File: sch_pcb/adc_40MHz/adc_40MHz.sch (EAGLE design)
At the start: 74 parts, among them IC1 AD9235BC, IC2 LT6600-15, IC3 LTC6254XMS, IC4 SN74LVC2G14DBV, IC5 LT1521XST, IC6 SN74LVC2G14DBV, X1 SMA-142-0701-851/861, X2 SMA-142-0701-851/861

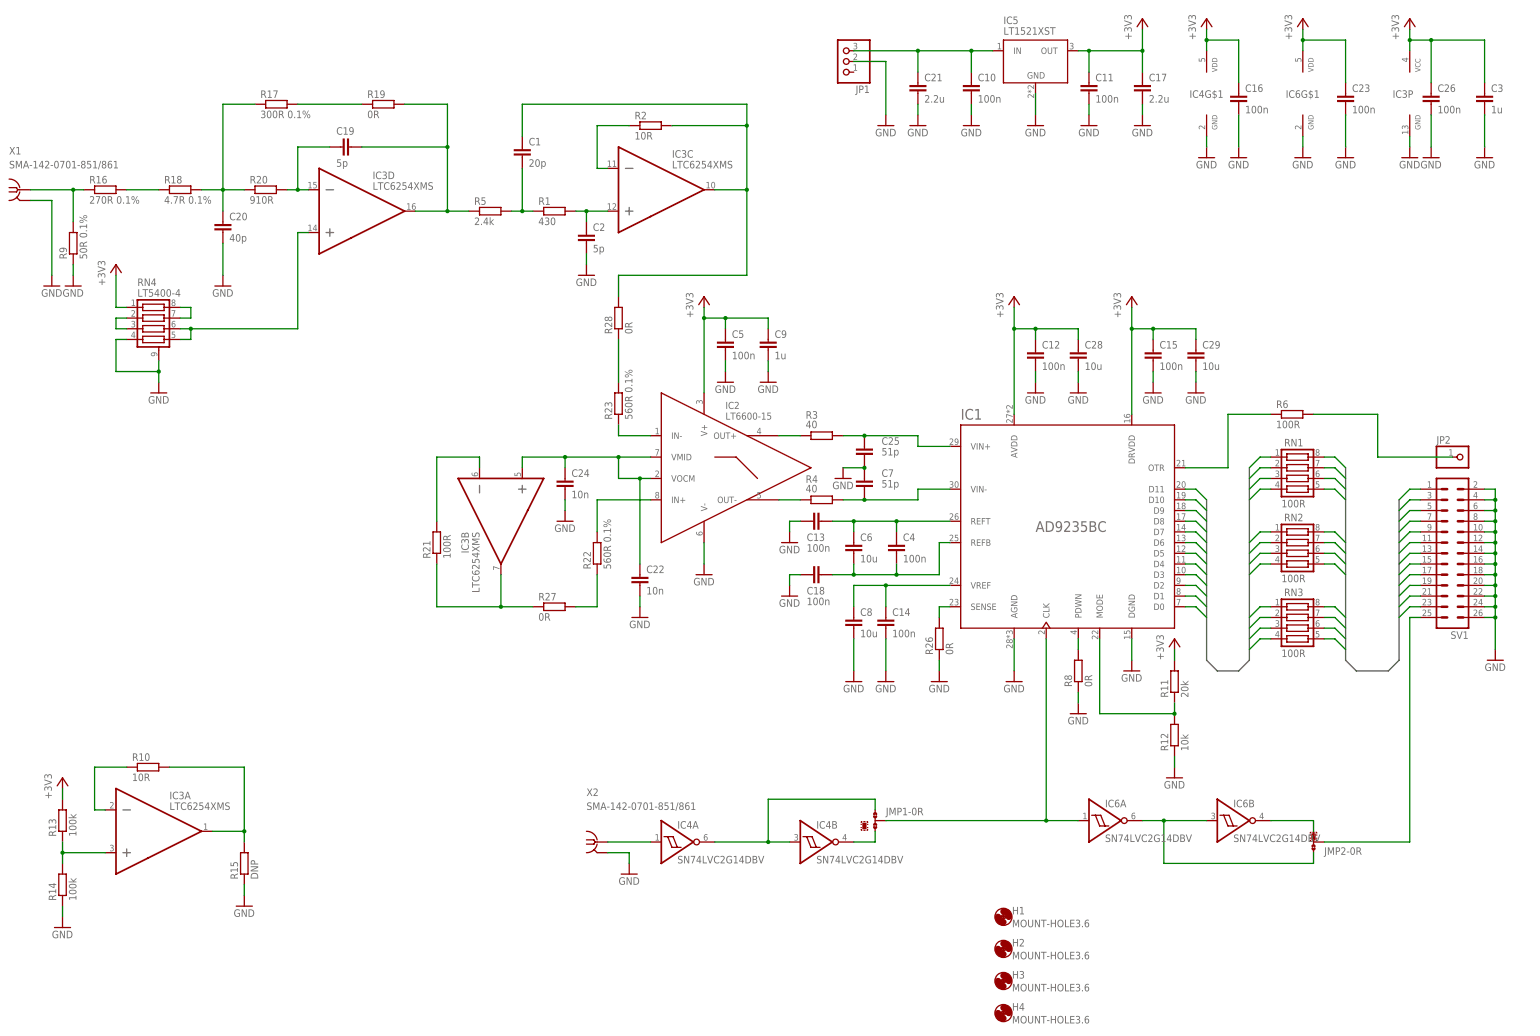
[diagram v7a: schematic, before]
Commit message: Dodano rezystory ustalające stan buforów. Sygnały w filrach skończone
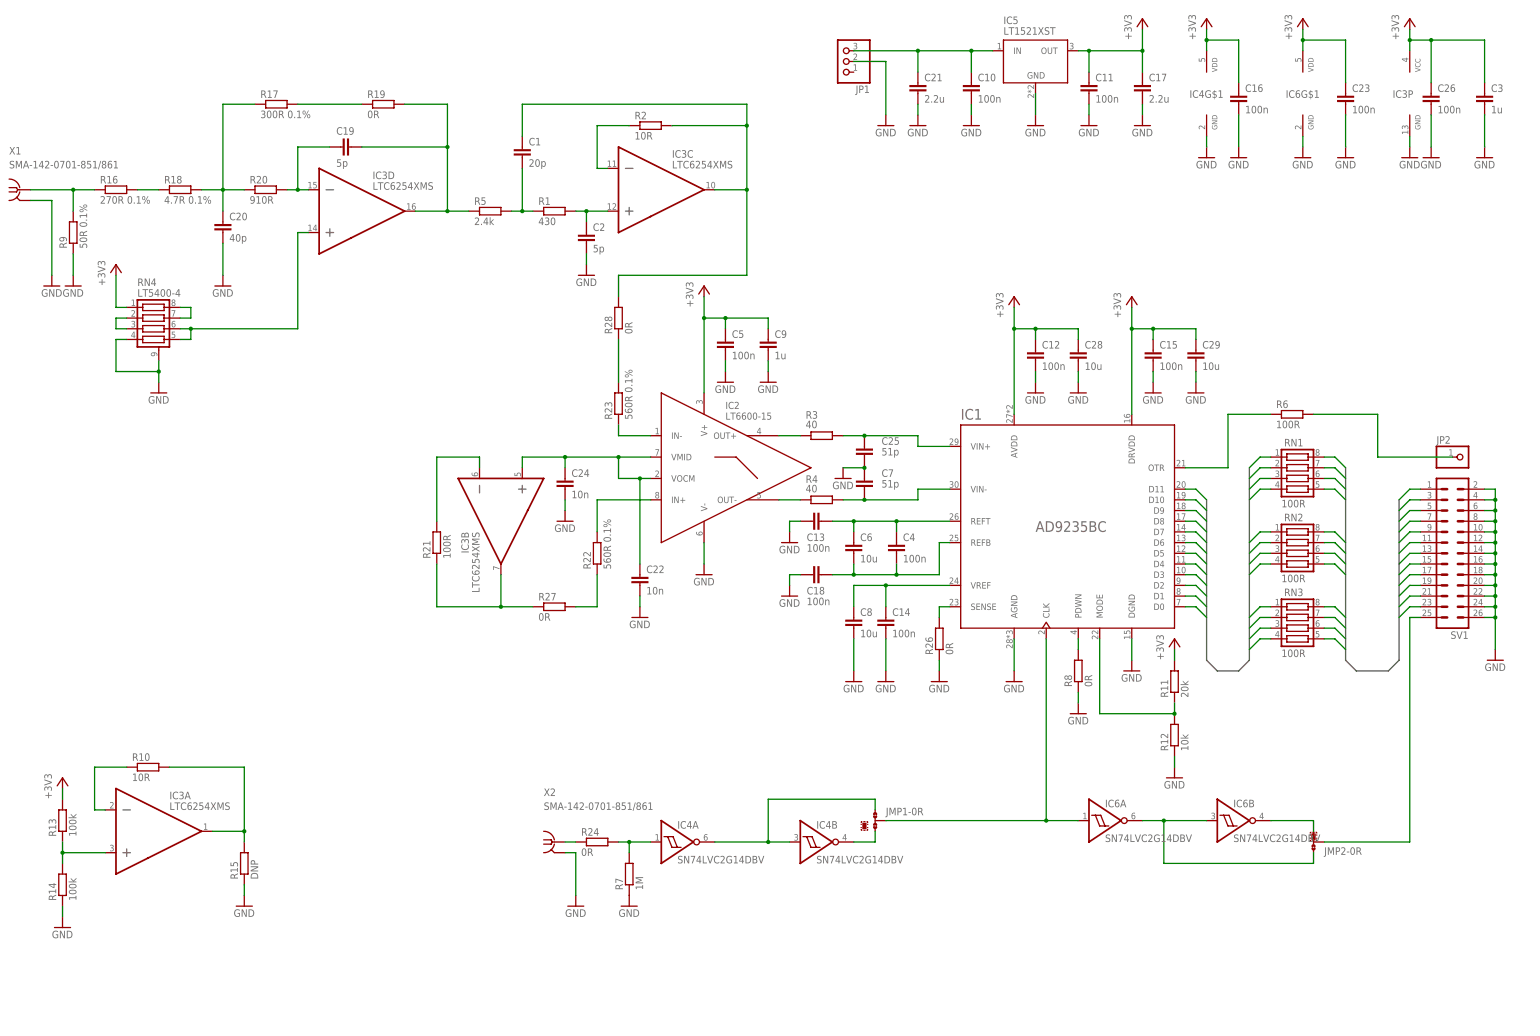
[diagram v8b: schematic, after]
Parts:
- removed H1, H2, H3, H4: MOUNT-HOLE3.6, holes:MOUNT-HOLE3.6
- added R24: 0R, rcl:R-EU_R0603
- added R7: 1M, rcl:R-EU_R0603
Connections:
- new net N$18: R24.1, X2.1
- new net SIGIN: R16.1, R9.2, X1.1
- net GND: now also R7.1
- net N$34: now also R24.2, R7.2; no longer X2.1
- net VIN: no longer R16.1, R9.2, X1.1
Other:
- moved on the sheet: R16, R9, X2
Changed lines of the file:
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@@
 <part name="C13" library="resistor" deviceset="C-EU" device="C0603K" value="100n"/>
 <part name="C18" library="resistor" deviceset="C-EU" device="C0603K" value="100n"/>
-<part name="H1" library="holes" deviceset="MOUNT-HOLE" device="3.6"/>
-<part name="H2" library="holes" deviceset="MOUNT-HOLE" device="3.6"/>
-<part name="H3" library="holes" deviceset="MOUNT-HOLE" device="3.6"/>
-<part name="H4" library="holes" deviceset="MOUNT-HOLE" device="3.6"/>
 <part name="C10" library="resistor" deviceset="C-EU" device="C0603K" value="100n"/>
 <part name="C11" library="resistor" deviceset="C-EU" device="C0603K" value="100n"/>
@@
 <part name="X2" library="con-coax" deviceset="SMA-" device="142-0701-851/861"/>
 <part name="C22" library="resistor" deviceset="C-EU" device="C0603K" value="10n"/>
+<part name="R7" library="rcl" deviceset="R-EU_" device="R0603" value="1M"/>
+<part name="GND42" library="supply1" deviceset="GND" device=""/>
+<part name="R24" library="rcl" deviceset="R-EU_" device="R0603" value="0R"/>
 </parts>
 <sheets>
@@
 <instance part="RN2" gate="G$1" x="320.04" y="111.76"/>
 <instance part="RN3" gate="G$1" x="320.04" y="93.98"/>
-<instance part="GND4" gate="1" x="165.1" y="40.64"/>
+<instance part="GND4" gate="1" x="152.4" y="33.02"/>
 <instance part="GND5" gate="1" x="27.94" y="180.34"/>
 <instance part="JP1" gate="A" x="215.9" y="233.68" rot="R180"/>
@@
 <instance part="GND11" gate="1" x="287.02" y="218.44"/>
 <instance part="GND12" gate="1" x="182.88" y="111.76"/>
-<instance part="+3V3" gate="G$1" x="182.88" y="177.8"/>
+<instance part="+3V3" gate="G$1" x="182.88" y="180.34"/>
 <instance part="JP2" gate="G$1" x="363.22" y="139.7"/>
 <instance part="R6" gate="G$1" x="322.58" y="149.86"/>
@@
 <instance part="GND23" gate="1" x="355.6" y="210.82"/>
 <instance part="GND24" gate="1" x="368.3" y="210.82"/>
-<instance part="R9" gate="G$1" x="33.02" y="190.5" rot="R90"/>
+<instance part="R9" gate="G$1" x="33.02" y="193.04" rot="R90"/>
 <instance part="GND25" gate="1" x="33.02" y="180.34"/>
 <instance part="R10" gate="G$1" x="50.8" y="66.04"/>
@@
 <instance part="GND28" gate="1" x="53.34" y="154.94"/>
 <instance part="+3V8" gate="G$1" x="43.18" y="185.42"/>
-<instance part="R16" gate="G$1" x="40.64" y="203.2"/>
+<instance part="R16" gate="G$1" x="43.18" y="203.2"/>
 <instance part="R17" gate="G$1" x="81.28" y="223.52"/>
 <instance part="C19" gate="G$1" x="96.52" y="213.36" smashed="yes" rot="R90">
@@
 <attribute name="VALUE" x="207.264" y="104.521" size="1.778" layer="96"/>
 </instance>
-<instance part="H1" gate="G$1" x="254" y="30.48"/>
-<instance part="H2" gate="G$1" x="254" y="22.86"/>
-<instance part="H3" gate="G$1" x="254" y="15.24"/>
-<instance part="H4" gate="G$1" x="254" y="7.62"/>
 <instance part="C10" gate="G$1" x="246.38" y="228.6"/>
 <instance part="C11" gate="G$1" x="274.32" y="228.6"/>
@@
 <attribute name="NAME" x="17.78" y="211.582" size="1.778" layer="95"/>
 </instance>
-<instance part="X2" gate="G1" x="157.48" y="48.26" smashed="yes">
-<attribute name="VALUE" x="154.94" y="55.88" size="1.778" layer="96"/>
-<attribute name="NAME" x="154.94" y="59.182" size="1.778" layer="95"/>
+<instance part="X2" gate="G1" x="147.32" y="48.26" smashed="yes">
+<attribute name="VALUE" x="144.78" y="55.88" size="1.778" layer="96"/>
+<attribute name="NAME" x="144.78" y="59.182" size="1.778" layer="95"/>
 </instance>
 <instance part="C22" gate="G$1" x="167.64" y="111.76"/>
+<instance part="R7" gate="G$1" x="165.1" y="40.64" rot="R90"/>
+<instance part="GND42" gate="1" x="165.1" y="33.02"/>
+<instance part="R24" gate="G$1" x="157.48" y="48.26"/>
 </instances>
 <busses>
@@
 </segment>
 <segment>
-<wire x1="160.02" y1="45.72" x2="165.1" y2="45.72" width="0.1524" layer="91"/>
+<wire x1="149.86" y1="45.72" x2="152.4" y2="45.72" width="0.1524" layer="91"/>
 <pinref part="GND4" gate="1" pin="GND"/>
-<wire x1="165.1" y1="45.72" x2="165.1" y2="43.18" width="0.1524" layer="91"/>
+<wire x1="152.4" y1="45.72" x2="152.4" y2="35.56" width="0.1524" layer="91"/>
 <pinref part="X2" gate="G1" pin="2"/>
 </segment>
@@
 <pinref part="R9" gate="G$1" pin="1"/>
 <pinref part="GND25" gate="1" pin="GND"/>
-<wire x1="33.02" y1="182.88" x2="33.02" y2="185.42" width="0.1524" layer="91"/>
+<wire x1="33.02" y1="182.88" x2="33.02" y2="187.96" width="0.1524" layer="91"/>
 </segment>
 <segment>
@@
 <wire x1="226.06" y1="88.9" x2="226.06" y2="96.52" width="0.1524" layer="91"/>
 </segment>
+<segment>
+<pinref part="R7" gate="G$1" pin="1"/>
+<pinref part="GND42" gate="1" pin="GND"/>
+</segment>
 </net>
 <net name="DAC_D11" class="0">
@@
 <wire x1="317.5" y1="96.52" x2="314.96" y2="96.52" width="0.1524" layer="91"/>
 <wire x1="314.96" y1="96.52" x2="312.42" y2="93.98" width="0.1524" layer="91"/>
-</segment>
-</net>
-<net name="VIN" class="0">
-<segment>
-<pinref part="IC5" gate="G$1" pin="IN"/>
-<wire x1="233.68" y1="236.22" x2="246.38" y2="236.22" width="0.1524" layer="91"/>
-<wire x1="246.38" y1="236.22" x2="251.46" y2="236.22" width="0.1524" layer="91"/>
-<wire x1="233.68" y1="231.14" x2="233.68" y2="236.22" width="0.1524" layer="91"/>
-<wire x1="246.38" y1="231.14" x2="246.38" y2="236.22" width="0.1524" layer="91"/>
-<junction x="246.38" y="236.22"/>
-<pinref part="C21" gate="G$1" pin="1"/>
-<pinref part="JP1" gate="A" pin="3"/>
-<wire x1="233.68" y1="236.22" x2="218.44" y2="236.22" width="0.1524" layer="91"/>
-<junction x="233.68" y="236.22"/>
-<pinref part="C10" gate="G$1" pin="1"/>
-</segment>
-<segment>
-<pinref part="R9" gate="G$1" pin="2"/>
-<wire x1="22.86" y1="203.2" x2="33.02" y2="203.2" width="0.1524" layer="91"/>
-<wire x1="33.02" y1="203.2" x2="33.02" y2="195.58" width="0.1524" layer="91"/>
-<pinref part="R16" gate="G$1" pin="1"/>
-<wire x1="35.56" y1="203.2" x2="33.02" y2="203.2" width="0.1524" layer="91"/>
-<junction x="33.02" y="203.2"/>
-<pinref part="X1" gate="G1" pin="1"/>
 </segment>
 </net>
@@
 </segment>
 <segment>
-<pinref part="+3V3" gate="G$1" pin="+3V3"/>
-<wire x1="182.88" y1="175.26" x2="182.88" y2="172.72" width="0.1524" layer="91"/>
-<pinref part="C5" gate="G$1" pin="1"/>
-<wire x1="182.88" y1="172.72" x2="182.88" y2="154.94" width="0.1524" layer="91"/>
-<wire x1="187.96" y1="170.18" x2="187.96" y2="172.72" width="0.1524" layer="91"/>
-<wire x1="187.96" y1="172.72" x2="182.88" y2="172.72" width="0.1524" layer="91"/>
-<junction x="182.88" y="172.72"/>
-<pinref part="IC2" gate="G$1" pin="V+"/>
-<wire x1="187.96" y1="172.72" x2="198.12" y2="172.72" width="0.1524" layer="91"/>
-<wire x1="198.12" y1="172.72" x2="198.12" y2="170.18" width="0.1524" layer="91"/>
-<junction x="187.96" y="172.72"/>
-<pinref part="C9" gate="G$1" pin="1"/>
-</segment>
-<segment>
 <pinref part="IC3" gate="P" pin="V+"/>
 <pinref part="+3V2" gate="G$1" pin="+3V3"/>
@@
 <pinref part="C23" gate="G$1" pin="1"/>
 </segment>
+<segment>
+<pinref part="C5" gate="G$1" pin="1"/>
+<wire x1="182.88" y1="172.72" x2="182.88" y2="154.94" width="0.1524" layer="91"/>
+<wire x1="187.96" y1="170.18" x2="187.96" y2="172.72" width="0.1524" layer="91"/>
+<wire x1="187.96" y1="172.72" x2="182.88" y2="172.72" width="0.1524" layer="91"/>
+<pinref part="IC2" gate="G$1" pin="V+"/>
+<wire x1="187.96" y1="172.72" x2="198.12" y2="172.72" width="0.1524" layer="91"/>
+<wire x1="198.12" y1="172.72" x2="198.12" y2="170.18" width="0.1524" layer="91"/>
+<junction x="187.96" y="172.72"/>
+<pinref part="C9" gate="G$1" pin="1"/>
+<wire x1="182.88" y1="177.8" x2="182.88" y2="172.72" width="0.1524" layer="91"/>
+<junction x="182.88" y="172.72"/>
+<pinref part="+3V3" gate="G$1" pin="+3V3"/>
+</segment>
 </net>
 <net name="N$6" class="0">
@@
 <pinref part="R16" gate="G$1" pin="2"/>
 <pinref part="R18" gate="G$1" pin="1"/>
-<wire x1="45.72" y1="203.2" x2="53.34" y2="203.2" width="0.1524" layer="91"/>
+<wire x1="48.26" y1="203.2" x2="53.34" y2="203.2" width="0.1524" layer="91"/>
 </segment>
 </net>
@@
 <net name="N$34" class="0">
 <segment>
-<wire x1="170.18" y1="48.26" x2="160.02" y2="48.26" width="0.1524" layer="91"/>
+<wire x1="170.18" y1="48.26" x2="165.1" y2="48.26" width="0.1524" layer="91"/>
 <pinref part="IC4" gate="A" pin="I"/>
-<pinref part="X2" gate="G1" pin="1"/>
+<pinref part="R7" gate="G$1" pin="2"/>
+<wire x1="165.1" y1="45.72" x2="165.1" y2="48.26" width="0.1524" layer="91"/>
+<pinref part="R24" gate="G$1" pin="2"/>
+<wire x1="162.56" y1="48.26" x2="165.1" y2="48.26" width="0.1524" layer="91"/>
+<junction x="165.1" y="48.26"/>
 </segment>
 </net>
@@
 </segment>
 </net>
+<net name="N$18" class="0">
+<segment>
+<pinref part="X2" gate="G1" pin="1"/>
+<pinref part="R24" gate="G$1" pin="1"/>
+<wire x1="149.86" y1="48.26" x2="152.4" y2="48.26" width="0.1524" layer="91"/>
+</segment>
+</net>
+<net name="VIN" class="0">
+<segment>
+<pinref part="JP1" gate="A" pin="3"/>
+<pinref part="C21" gate="G$1" pin="1"/>
+<wire x1="218.44" y1="236.22" x2="233.68" y2="236.22" width="0.1524" layer="91"/>
+<wire x1="233.68" y1="236.22" x2="233.68" y2="231.14" width="0.1524" layer="91"/>
+<pinref part="C10" gate="G$1" pin="1"/>
+<wire x1="233.68" y1="236.22" x2="246.38" y2="236.22" width="0.1524" layer="91"/>
+<wire x1="246.38" y1="236.22" x2="246.38" y2="231.14" width="0.1524" layer="91"/>
+<junction x="233.68" y="236.22"/>
+<pinref part="IC5" gate="G$1" pin="IN"/>
+<wire x1="246.38" y1="236.22" x2="251.46" y2="236.22" width="0.1524" layer="91"/>
+<junction x="246.38" y="236.22"/>
+</segment>
+</net>
+<net name="SIGIN" class="0">
+<segment>
+<pinref part="X1" gate="G1" pin="1"/>
+<pinref part="R16" gate="G$1" pin="1"/>
+<wire x1="22.86" y1="203.2" x2="33.02" y2="203.2" width="0.1524" layer="91"/>
+<pinref part="R9" gate="G$1" pin="2"/>
+<wire x1="33.02" y1="203.2" x2="38.1" y2="203.2" width="0.1524" layer="91"/>
+<wire x1="33.02" y1="198.12" x2="33.02" y2="203.2" width="0.1524" layer="91"/>
+<junction x="33.02" y="203.2"/>
+</segment>
+</net>
